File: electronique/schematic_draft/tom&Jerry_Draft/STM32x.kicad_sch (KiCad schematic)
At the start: 59 parts, among them J501 Conn_ST_STDC14, SW1 SW_Push, SW2 SW_Push, SW3 SW_Push, SW4 SW_Push, U502 STM32G431CBU6, Y1 16MHz

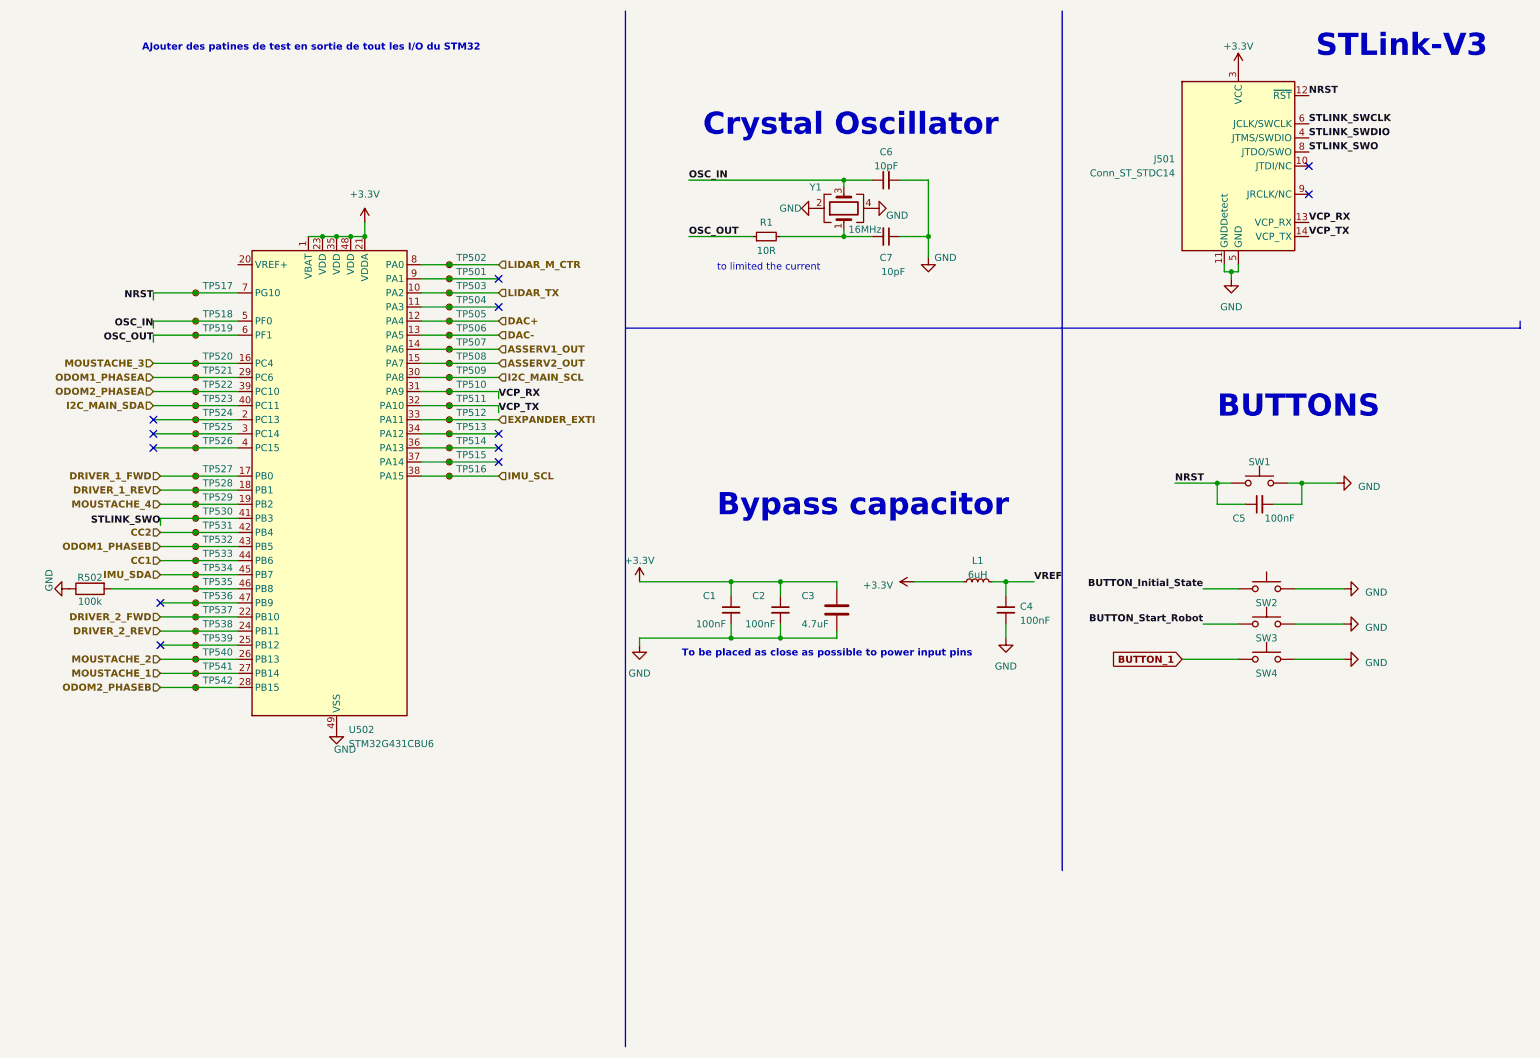
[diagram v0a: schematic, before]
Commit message: STM32 KiCAD v2.0 x CubeIDE - Pin definitif + schematic reviewed
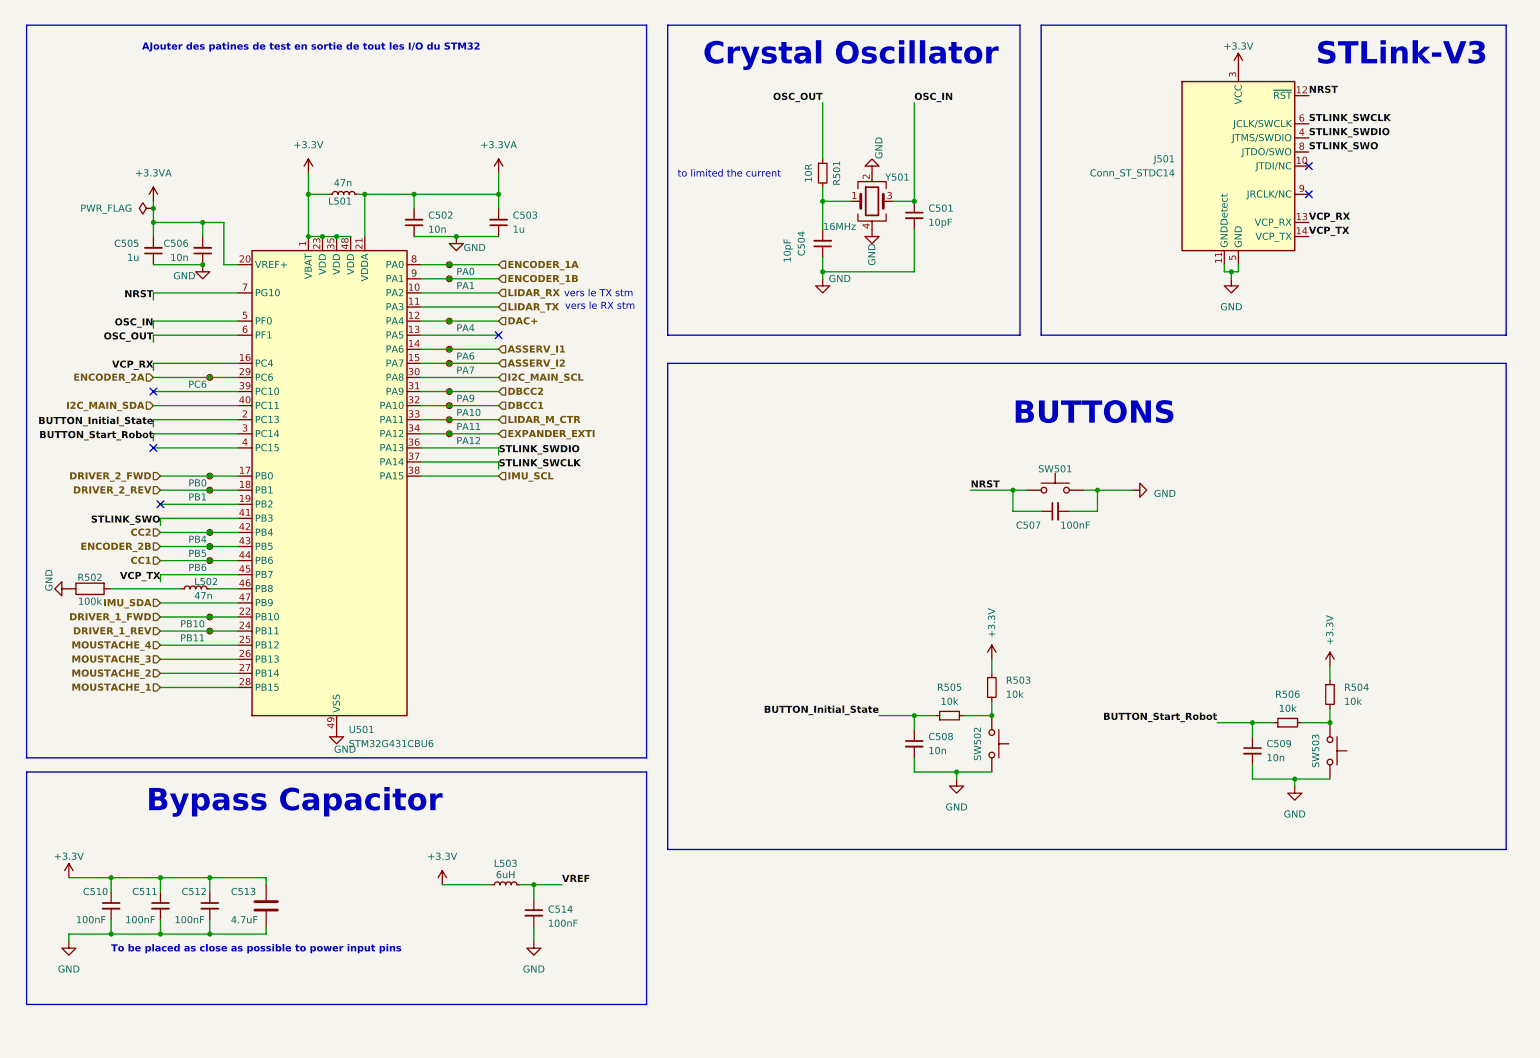
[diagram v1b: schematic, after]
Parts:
- removed C6, C7: 10pF, Capacitor_SMD:C_0603_1608Metric_Pad1.08x0.95mm_HandSolder, symbol Device:C_Small
- removed R1: 10R, Resistor_SMD:R_0603_1608Metric_Pad0.98x0.95mm_HandSolder, symbol Device:R_Small
- removed SW2, SW3, SW4: SW_Push, Button_Switch_SMD:SW_SPST_B3U-1000P, symbol Switch:SW_Push
- removed TP503, TP506, TP513, TP514, TP515, TP518, TP519, TP520, TP522, TP523, TP524, TP525, TP526, TP527, TP528, TP529, TP530, TP534, TP535, TP536, TP537, TP538, TP539, TP540, TP541, TP542: TestPoint_Small, symbol Connector:TestPoint_Small
- removed Y1: 16MHz, Crystal:Crystal_SMD_3225-4Pin_3.2x2.5mm, symbol Device:Crystal_GND24
- added C501, C504: 10pF, Capacitor_SMD:C_0603_1608Metric_Pad1.08x0.95mm_HandSolder, symbol Device:C_Small
- added C502, C506, C508, C509: 10n, symbol Device:C_Small
- added C503, C505: 1u, symbol Device:C_Small
- added C510: 100nF, Capacitor_SMD:C_0603_1608Metric_Pad1.08x0.95mm_HandSolder, symbol Device:C_Small
- added L501, L502: 47n, symbol Device:L_Small
- added R501: 10R, Resistor_SMD:R_0603_1608Metric_Pad0.98x0.95mm_HandSolder, symbol Device:R_Small
- added R503, R504, R505, R506: 10k, symbol Device:R_Small
- added SW502, SW503: SW_Push, Button_Switch_SMD:SW_SPST_B3U-1000P, symbol Switch:SW_Push
- added TP505: PA7, symbol Connector:TestPoint_Small
- added Y501: 16MHz, Crystal:Crystal_SMD_3225-4Pin_3.2x2.5mm, symbol Device:Crystal_GND24
- TP501: value TestPoint_Small -> PA0
- TP502: value TestPoint_Small -> PA1
- TP503: renamed from TP505; value TestPoint_Small -> PA4
- TP504: value TestPoint_Small -> PA6
- TP506: renamed from TP521; value TestPoint_Small -> PC6
- TP507: value TestPoint_Small -> PA9
- TP508: value TestPoint_Small -> PA10
- TP509: value TestPoint_Small -> PA11
- TP510: value TestPoint_Small -> PA12
- TP511: value TestPoint_Small -> PB0
- TP512: value TestPoint_Small -> PB1
- TP513: renamed from TP531; value TestPoint_Small -> PB4
- TP514: renamed from TP532; value TestPoint_Small -> PB5
- TP515: renamed from TP533; value TestPoint_Small -> PB6
- TP516: value TestPoint_Small -> PB10
- TP517: value TestPoint_Small -> PB11
- renumbered C5 to C507, C1 to C511, C2 to C512, C3 to C513, C4 to C514, L1 to L503, SW1 to SW501, U502 to U501
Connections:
- net ODOM2_PHASEB is gone; now on net MOUSTACHE_1: U501.28 (PB15)
- net +3.3V: now also C510.1, L501.2, R503.1, R504.1; no longer U501.21 (VDDA)
- net BUTTON_Initial_State: now also U501.2 (PC13), C508.1, R505.1
- net BUTTON_Start_Robot: now also U501.3 (PC14), C509.1, R506.1
- net DRIVER_1_FWD: now also TP516.1, U501.22 (PB10); no longer U501.17 (PB0)
- net DRIVER_1_REV: now also TP517.1, U501.24 (PB11); no longer U501.18 (PB1)
- net DRIVER_2_FWD: now also TP511.1, U501.17 (PB0); no longer U501.22 (PB10)
- net DRIVER_2_REV: now also TP512.1, U501.18 (PB1); no longer U501.24 (PB11)
- net EXPANDER_EXTI: now also TP510.1, U501.34 (PA12); no longer TP512.1, U501.33 (PA11)
- net GND: now also C501.2, C502.1, C503.1, C504.1, C505.1, C506.1, C508.2, C509.2, C510.2, SW502.1, SW503.1, Y501.2, Y501.4
- net I2C_MAIN_SCL: no longer TP509.1
- net IMU_SCL: no longer TP516.1
- net IMU_SDA: now also U501.47 (PB9); no longer U501.45 (PB7)
- net LIDAR_M_CTR: now also TP509.1, U501.33 (PA11); no longer TP502.1, U501.8 (PA0)
- net LIDAR_TX: now also U501.11 (PA3); no longer U501.10 (PA2)
- net MOUSTACHE_1: no longer U501.27 (PB14)
- net MOUSTACHE_2: now also U501.27 (PB14); no longer U501.26 (PB13)
- net MOUSTACHE_3: now also U501.26 (PB13); no longer U501.16 (PC4)
- net MOUSTACHE_4: now also U501.25 (PB12); no longer U501.19 (PB2)
- net NRST: no longer TP517.1
- net OSC_IN: now also C501.1, Y501.3
- net OSC_OUT: now also R501.1
- net STLINK_SWCLK: now also U501.37 (PA14)
- net STLINK_SWDIO: now also U501.36 (PA13)
- net VCP_RX: now also U501.16 (PC4); no longer TP510.1, U501.31 (PA9)
- net VCP_TX: now also U501.45 (PB7); no longer TP511.1, U501.32 (PA10)
- net at R502.2: now also L502.2; no longer U501.46 (PB8)
- net ENCODER_1A: now reaches TP501.1
- net ENCODER_1A: now also U501.8 (PA0); no longer U501.9 (PA1)
- net ASSERV_I1: now reaches TP504.1
- net ASSERV_I1: now also U501.14 (PA6); no longer U501.11 (PA3)
- net +3.3VA: now reaches U501.20 (VREF+)
- net +3.3VA: now also U501.21 (VDDA), C502.2, C503.2, C505.2, C506.2, L501.1
- net ASSERV1_OUT renamed DBCC2
- net DBCC2: now also U501.31 (PA9); no longer U501.14 (PA6)
- net ASSERV2_OUT renamed ASSERV_I2
- net ASSERV_I2: now also TP505.1; no longer TP508.1
- net DAC-: no longer names the net of U501.13 (PA5)
- net ODOM1_PHASEA renamed ENCODER_2A
- net ODOM1_PHASEB renamed ENCODER_2B
- net ODOM2_PHASEA: no longer names the net of U501.39 (PC10)
- new net: R504.2, R506.2, SW503.2
- new net: R503.2, R505.2, SW502.2
- new net: C504.2, R501.2, Y501.1
- new net: L502.1, U501.46 (PB8)
- new net DBCC1: TP508.1, U501.32 (PA10)
- new net ENCODER_1B: TP502.1, U501.9 (PA1)
- new net LIDAR_RX: U501.10 (PA2)
- no-connect marks 12 -> 6
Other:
- note added: "Bypass Capacitor"
- note added: "vers le RX stm"
- note added: "vers le TX stm"
- note removed: "Bypass capacitor"
- moved on the sheet: C507, C511, C512, C513, C514, L503, SW501

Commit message: Adding footprint V0.1
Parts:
- C501, C504: value 10pF -> 10p; footprint Capacitor_SMD:C_0603_1608Metric_Pad1.08x0.95mm_HandSolder -> Capacitor_SMD:C_0402_1005Metric
- C502, C506, C508, C509: footprint (none) -> Capacitor_SMD:C_0402_1005Metric
- C503, C505: footprint (none) -> Capacitor_SMD:C_0603_1608Metric
- C507: footprint Capacitor_SMD:C_0603_1608Metric_Pad1.08x0.95mm_HandSolder -> Capacitor_SMD:C_0402_1005Metric
- C510, C511, C512, C514: value 100nF -> 100n; footprint Capacitor_SMD:C_0603_1608Metric_Pad1.08x0.95mm_HandSolder -> Capacitor_SMD:C_0402_1005Metric
- C513: value 4.7uF -> 4.7u; footprint Capacitor_SMD:C_0603_1608Metric_Pad1.08x0.95mm_HandSolder -> Capacitor_SMD:C_0603_1608Metric
- J501: footprint (none) -> Connector_PinHeader_1.27mm:PinHeader_2x07_P1.27mm_Vertical_SMD
- L501: value 47n -> 39n; footprint (none) -> Inductor_SMD:L_0603_1608Metric_Pad1.05x0.95mm_HandSolder
- L502: footprint (none) -> Inductor_SMD:L_0603_1608Metric_Pad1.05x0.95mm_HandSolder
- L503: value 6uH -> 6u
- R501: footprint Resistor_SMD:R_0603_1608Metric_Pad0.98x0.95mm_HandSolder -> Resistor_SMD:R_0402_1005Metric
- R502, R503, R504, R505, R506: footprint (none) -> Resistor_SMD:R_0402_1005Metric
- SW501, SW502, SW503: footprint Button_Switch_SMD:SW_SPST_B3U-1000P -> Button_Switch_SMD:SW_Push_1P1T_NO_6x6mm_H9.5mm
- TP501, TP502, TP503, TP504, TP505, TP506, TP507, TP508, TP509, TP510, TP511, TP512, TP513, TP514, TP515, TP516, TP517: footprint (none) -> Test_Point:TestPoint_Pad_D1.5mm
- U501: footprint Package_DFN_QFN:QFN-48-1EP_7x7mm_P0.5mm_EP5.6x5.6mm -> Package_DFN_QFN:QFN-48-1EP_7x7mm_P0.5mm_EP5.1x5.1mm
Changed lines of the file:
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@@
 			)
 		)
-		(property "Footprint" ""
+		(property "Footprint" "Test_Point:TestPoint_Pad_D1.5mm"
 			(at 97.79 85.09 0)
 			(effects
@@
 			)
 		)
-		(property "Footprint" ""
+		(property "Footprint" "Resistor_SMD:R_0402_1005Metric"
 			(at 251.46 134.62 0)
 			(effects
@@
 			)
 		)
-		(property "Footprint" ""
+		(property "Footprint" "Capacitor_SMD:C_0603_1608Metric"
 			(at 39.37 54.61 0)
 			(effects
@@
 			)
 		)
-		(property "Value" "10pF"
+		(property "Value" "10p"
 			(at 179.07 49.5362 0)
 			(effects
@@
 			)
 		)
-		(property "Footprint" "Capacitor_SMD:C_0603_1608Metric_Pad1.08x0.95mm_HandSolder"
+		(property "Footprint" "Capacitor_SMD:C_0402_1005Metric"
 			(at 176.53 48.26 0)
 			(effects
@@
 			)
 		)
-		(property "Footprint" "Button_Switch_SMD:SW_SPST_B3U-1000P"
+		(property "Footprint" "Button_Switch_SMD:SW_Push_1P1T_NO_6x6mm_H9.5mm"
 			(at 201.93 92.71 0)
 			(effects
@@
 			)
 		)
-		(property "Footprint" ""
+		(property "Footprint" "Test_Point:TestPoint_Pad_D1.5mm"
 			(at 54.61 107.95 0)
 			(effects
@@
 			)
 		)
-		(property "Footprint" ""
+		(property "Footprint" "Test_Point:TestPoint_Pad_D1.5mm"
 			(at 97.79 87.63 0)
 			(effects
@@
 			)
 		)
-		(property "Footprint" ""
+		(property "Footprint" "Resistor_SMD:R_0402_1005Metric"
 			(at 27.94 113.792 90)
 			(effects
@@
 			)
 		)
-		(property "Footprint" "Capacitor_SMD:C_0603_1608Metric_Pad1.08x0.95mm_HandSolder"
+		(property "Footprint" "Capacitor_SMD:C_0402_1005Metric"
 			(at 201.93 101.6 0)
 			(effects
@@
 			)
 		)
-		(property "Footprint" ""
+		(property "Footprint" "Test_Point:TestPoint_Pad_D1.5mm"
 			(at 54.61 77.47 0)
 			(effects
@@
 			)
 		)
-		(property "Footprint" ""
+		(property "Footprint" "Test_Point:TestPoint_Pad_D1.5mm"
 			(at 97.79 59.69 0)
 			(effects
@@
 			)
 		)
-		(property "Value" "100nF"
+		(property "Value" "100n"
 			(at 43.18 175.26 0)
 			(effects
@@
 			)
 		)
-		(property "Footprint" "Capacitor_SMD:C_0603_1608Metric_Pad1.08x0.95mm_HandSolder"
+		(property "Footprint" "Capacitor_SMD:C_0402_1005Metric"
 			(at 49.53 172.72 0)
 			(effects
@@
 			)
 		)
-		(property "Footprint" "Button_Switch_SMD:SW_SPST_B3U-1000P"
+		(property "Footprint" "Button_Switch_SMD:SW_Push_1P1T_NO_6x6mm_H9.5mm"
 			(at 195.58 143.51 0)
 			(effects
@@
 			)
 		)
-		(property "Footprint" "Button_Switch_SMD:SW_SPST_B3U-1000P"
+		(property "Footprint" "Button_Switch_SMD:SW_Push_1P1T_NO_6x6mm_H9.5mm"
 			(at 256.54 144.78 0)
 			(effects
@@
 			)
 		)
-		(property "Value" "100nF"
+		(property "Value" "100n"
 			(at 25.4 175.26 0)
 			(effects
@@
 			)
 		)
-		(property "Footprint" "Capacitor_SMD:C_0603_1608Metric_Pad1.08x0.95mm_HandSolder"
+		(property "Footprint" "Capacitor_SMD:C_0402_1005Metric"
 			(at 31.75 172.72 0)
 			(effects
@@
 			)
 		)
-		(property "Footprint" ""
+		(property "Footprint" "Test_Point:TestPoint_Pad_D1.5mm"
 			(at 54.61 105.41 0)
 			(effects
@@
 			)
 		)
-		(property "Value" "10pF"
+		(property "Value" "10p"
 			(at 153.67 54.61 90)
 			(effects
@@
 			)
 		)
-		(property "Footprint" "Capacitor_SMD:C_0603_1608Metric_Pad1.08x0.95mm_HandSolder"
+		(property "Footprint" "Capacitor_SMD:C_0402_1005Metric"
 			(at 160.02 53.34 0)
 			(effects
@@
 			)
 		)
-		(property "Footprint" ""
+		(property "Footprint" "Connector_PinHeader_1.27mm:PinHeader_2x07_P1.27mm_Vertical_SMD"
 			(at 234.95 39.37 0)
 			(effects
@@
 			)
 		)
-		(property "Footprint" ""
+		(property "Footprint" "Test_Point:TestPoint_Pad_D1.5mm"
 			(at 54.61 97.79 0)
 			(effects
@@
 			)
 		)
-		(property "Footprint" ""
+		(property "Footprint" "Test_Point:TestPoint_Pad_D1.5mm"
 			(at 97.79 74.93 0)
 			(effects
@@
 			)
 		)
-		(property "Footprint" ""
+		(property "Footprint" "Test_Point:TestPoint_Pad_D1.5mm"
 			(at 97.79 57.15 0)
 			(effects
@@
 			)
 		)
-		(property "Footprint" ""
+		(property "Footprint" "Capacitor_SMD:C_0603_1608Metric"
 			(at 101.6 49.53 0)
 			(effects
@@
 			)
 		)
-		(property "Footprint" ""
+		(property "Footprint" "Capacitor_SMD:C_0402_1005Metric"
 			(at 176.53 143.51 0)
 			(effects
@@
 			)
 		)
-		(property "Footprint" ""
+		(property "Footprint" "Capacitor_SMD:C_0402_1005Metric"
 			(at 86.36 49.53 0)
 			(effects
@@
 			)
 		)
-		(property "Value" "6uH"
+		(property "Value" "6u"
 			(at 102.87 167.132 90)
 			(effects
@@
 			)
 		)
-		(property "Footprint" ""
+		(property "Footprint" "Test_Point:TestPoint_Pad_D1.5mm"
 			(at 97.79 72.39 0)
 			(effects
@@
 			)
 		)
-		(property "Footprint" ""
+		(property "Footprint" "Capacitor_SMD:C_0402_1005Metric"
 			(at 237.49 144.78 0)
 			(effects
@@
 			)
 		)
-		(property "Footprint" "Package_DFN_QFN:QFN-48-1EP_7x7mm_P0.5mm_EP5.6x5.6mm"
+		(property "Footprint" "Package_DFN_QFN:QFN-48-1EP_7x7mm_P0.5mm_EP5.1x5.1mm"
 			(at 57.15 138.43 0)
 			(effects
@@
 			)
 		)
-		(property "Footprint" ""
+		(property "Footprint" "Resistor_SMD:R_0402_1005Metric"
 			(at 243.84 139.7 0)
 			(effects
@@
 			)
 		)
-		(property "Footprint" ""
+		(property "Footprint" "Inductor_SMD:L_0603_1608Metric_Pad1.05x0.95mm_HandSolder"
 			(at 46.99 115.57 0)
 			(effects
@@
 			)
 		)
-		(property "Footprint" ""
+		(property "Footprint" "Test_Point:TestPoint_Pad_D1.5mm"
 			(at 54.61 120.65 0)
 			(effects
@@
 			)
 		)
-		(property "Footprint" ""
+		(property "Footprint" "Resistor_SMD:R_0402_1005Metric"
 			(at 182.88 138.43 0)
 			(effects
@@
 			)
 		)
-		(property "Footprint" ""
+		(property "Footprint" "Test_Point:TestPoint_Pad_D1.5mm"
 			(at 54.61 110.49 0)
 			(effects
@@
 			)
 		)
-		(property "Value" "100nF"
+		(property "Value" "100n"
 			(at 34.29 175.26 0)
 			(effects
@@
 			)
 		)
-		(property "Footprint" "Capacitor_SMD:C_0603_1608Metric_Pad1.08x0.95mm_HandSolder"
+		(property "Footprint" "Capacitor_SMD:C_0402_1005Metric"
 			(at 40.64 172.72 0)
 			(effects
@@
 			)
 		)
-		(property "Value" "4.7uF"
+		(property "Value" "4.7u"
 			(at 53.34 175.26 0)
 			(effects
@@
 			)
 		)
-		(property "Footprint" "Capacitor_SMD:C_0603_1608Metric_Pad1.08x0.95mm_HandSolder"
+		(property "Footprint" "Capacitor_SMD:C_0603_1608Metric"
 			(at 60.6552 176.53 0)
 			(effects
@@
 			)
 		)
-		(property "Footprint" ""
+		(property "Footprint" "Test_Point:TestPoint_Pad_D1.5mm"
 			(at 97.79 80.01 0)
 			(effects
@@
 		(fields_autoplaced yes)
 		(property "Reference" "C514"
-			(at 110.49 173.3613 0)
+			(at 110.49 172.7262 0)
 			(effects
 				(font
@@
 			)
 		)
-		(property "Value" "100nF"
-			(at 110.49 175.9013 0)
+		(property "Value" "100n"
+			(at 110.49 175.2662 0)
 			(effects
 				(font
@@
 			)
 		)
-		(property "Footprint" "Capacitor_SMD:C_0603_1608Metric_Pad1.08x0.95mm_HandSolder"
+		(property "Footprint" "Capacitor_SMD:C_0402_1005Metric"
 			(at 107.95 173.99 0)
 			(effects
@@
 			)
 		)
-		(property "Footprint" ""
+		(property "Footprint" "Test_Point:TestPoint_Pad_D1.5mm"
 			(at 54.61 123.19 0)
 			(effects
@@
 			)
 		)
-		(property "Footprint" ""
+		(property "Footprint" "Test_Point:TestPoint_Pad_D1.5mm"
 			(at 54.61 95.25 0)
 			(effects
@@
 			)
 		)
-		(property "Footprint" ""
+		(property "Footprint" "Test_Point:TestPoint_Pad_D1.5mm"
 			(at 97.79 82.55 0)
 			(effects
@@
 			)
 		)
-		(property "Footprint" ""
+		(property "Footprint" "Test_Point:TestPoint_Pad_D1.5mm"
 			(at 97.79 67.31 0)
 			(effects
@@
 			)
 		)
-		(property "Value" "47n"
+		(property "Value" "39n"
 			(at 71.882 42.418 90)
 			(effects
@@
 			)
 		)
-		(property "Footprint" ""
+		(property "Footprint" "Inductor_SMD:L_0603_1608Metric_Pad1.05x0.95mm_HandSolder"
 			(at 73.66 44.45 0)
 			(effects
@@
 			)
 		)
-		(property "Footprint" ""
+		(property "Footprint" "Resistor_SMD:R_0402_1005Metric"
 			(at 190.5 133.35 0)
 			(effects
@@
 			)
 		)
-		(property "Footprint" ""
+		(property "Footprint" "Capacitor_SMD:C_0402_1005Metric"
 			(at 48.26 54.61 0)
 			(effects
@@
 			)
 		)
-		(property "Footprint" "Resistor_SMD:R_0603_1608Metric_Pad0.98x0.95mm_HandSolder"
+		(property "Footprint" "Resistor_SMD:R_0402_1005Metric"
 			(at 160.02 40.64 0)
 			(effects

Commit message: Ajout V2 TOF + MultiPCB Panalize
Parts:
- renumbered C510 to C501, C505 to C502, C511 to C503, C506 to C504, C512 to C505, C513 to C506, C502 to C507, C503 to C508, C514 to C509, C504 to C510, C501 to C511, C508 to C512, C507 to C513, C509 to C514, L502 to L501, L501 to L502, R502 to R501, R501 to R502, R505 to R503, R503 to R504, R506 to R505, R504 to R506, SW502 to SW501, SW501 to SW502, TP506 to TP501, TP511 to TP502, TP512 to TP503, TP513 to TP504, TP514 to TP505, TP515 to TP506, TP516 to TP507, TP517 to TP508, TP501 to TP509, TP502 to TP510, TP503 to TP511, TP504 to TP512, TP505 to TP513, TP507 to TP514, TP508 to TP515, TP509 to TP516, TP510 to TP517

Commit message: Try some placement and routing
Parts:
- removed C509: 100n, Capacitor_SMD:C_0402_1005Metric, symbol Device:C_Small
- removed L503: 6u, Inductor_SMD:L_0603_1608Metric_Pad1.05x0.95mm_HandSolder, symbol Device:L_Small

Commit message: Routage Signal Complet
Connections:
- net DRIVER_1_FWD: now also TP508.1, U501.24 (PB11); no longer TP507.1, U501.22 (PB10)
- net DRIVER_1_REV: now also TP507.1, U501.22 (PB10); no longer TP508.1, U501.24 (PB11)
- net ENCODER_1A: now also TP510.1, U501.9 (PA1); no longer TP509.1, U501.8 (PA0)
- net ENCODER_1B: now also TP509.1, U501.8 (PA0); no longer TP510.1, U501.9 (PA1)
- net MOUSTACHE_1: now also U501.27 (PB14); no longer U501.28 (PB15)
- net MOUSTACHE_2: now also U501.26 (PB13); no longer U501.27 (PB14)
- net MOUSTACHE_3: now also U501.25 (PB12); no longer U501.26 (PB13)
- net MOUSTACHE_4: now also U501.28 (PB15); no longer U501.25 (PB12)
